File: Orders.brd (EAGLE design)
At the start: 160 x 100 mm, 5 parts, among them J1 10104111-0001LF

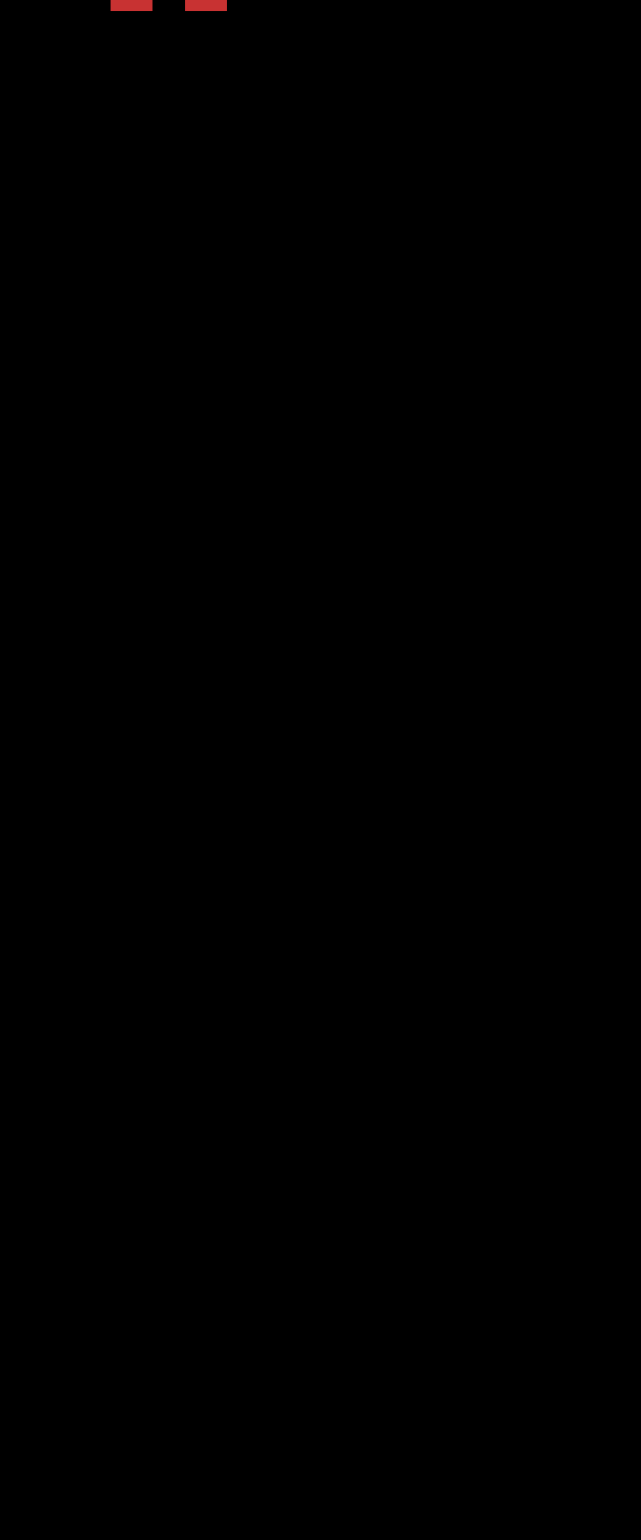
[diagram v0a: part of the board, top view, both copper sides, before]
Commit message: Added I2C pull-up resistances
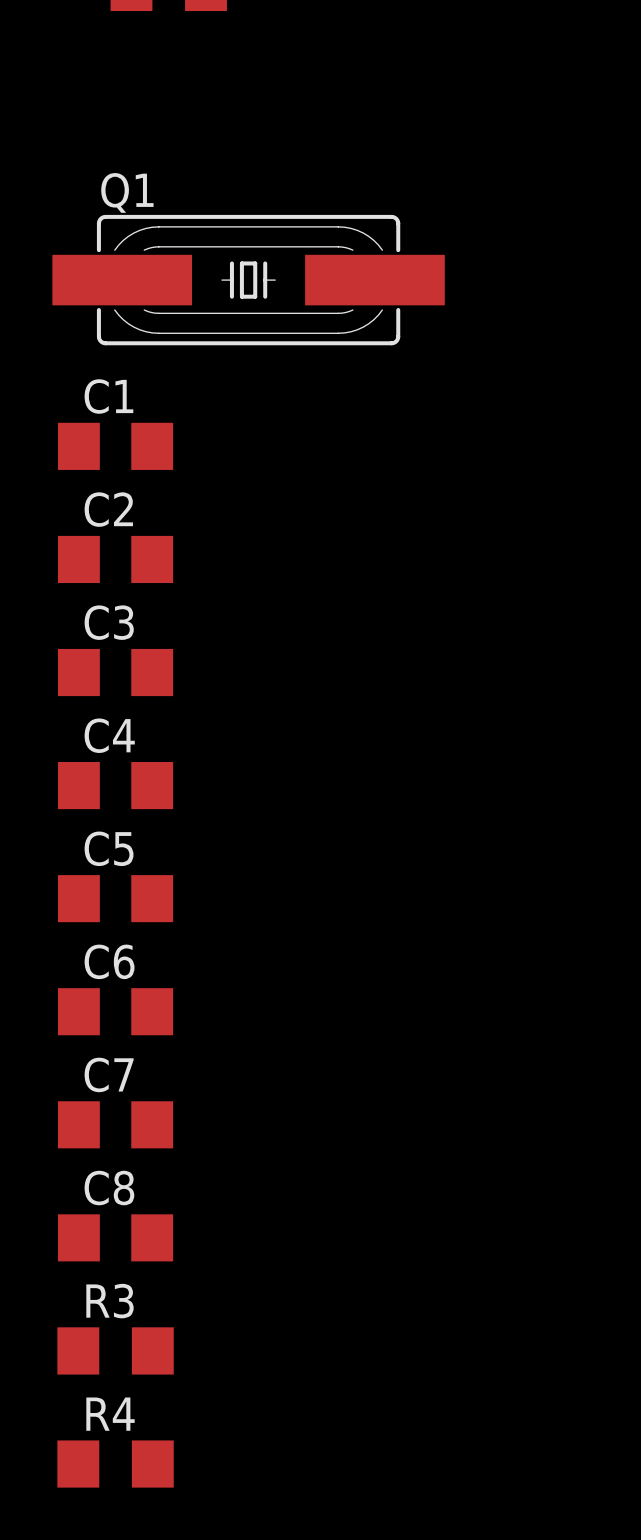
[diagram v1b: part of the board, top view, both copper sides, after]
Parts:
- added C1, C2, C3, C4, C5, C6, C7, C8: (no value), rcl:C1206
- added Q1: (no value), adafruit:HC49UP
- added R3, R4: (no value), rcl:R1206
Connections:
- new net N$3: C1.1, Q1.2, U$1.17
- new net N$4: C2.1, Q1.1, U$1.16
- new net N$5: C3.1, U$1.6
- net +5V: now also C4.1, C5.1, C6.1, C7.1, C8.1, R3.2, R4.2, U$1.14, U$1.2, U$1.24, U$1.34, U$1.44, U$1.7
- net D+: now also U$1.4
- net D-: now also U$1.3
- net GND: now also C1.2, C2.2, C3.2, C4.2, C5.2, C6.2, C7.2, C8.2, U$1.15, U$1.23, U$1.35, U$1.43, U$1.5
- net SCL: now also R3.1
- net SDA: now also R4.1

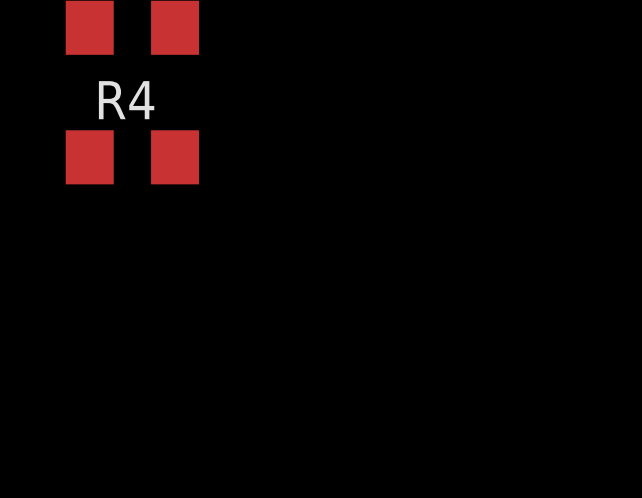
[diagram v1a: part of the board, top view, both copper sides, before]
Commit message: Added passives for uC
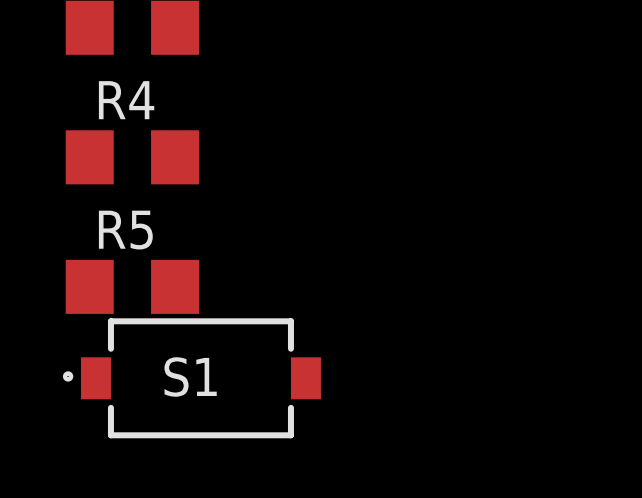
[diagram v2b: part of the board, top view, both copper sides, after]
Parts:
- added R5: (no value), rcl:R1206
- added S1: KSR231GLFS, Switch:KSR
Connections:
- new net N$6: R5.2, S1.2, U$1.13
- net +5V: now also R5.1
- net GND: now also S1.1
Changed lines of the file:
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@@
 <attribute name="VALUE" x="-50.292" y="-81.788" size="1.27" layer="27"/>
+</element>
+<element name="R5" library="rcl" library_urn="urn:adsk.eagle:library:334" package="R1206" package3d_urn="urn:adsk.eagle:package:23540/2" value="" x="-49.022" y="-83.566" smashed="yes">
+<attribute name="NAME" x="-50.292" y="-82.296" size="1.27" layer="25"/>
+<attribute name="POPULARITY" value="41" x="-49.022" y="-83.566" size="1.778" layer="27" display="off"/>
+<attribute name="SPICEPREFIX" value="R" x="-49.022" y="-83.566" size="1.778" layer="27" display="off"/>
+<attribute name="VALUE" x="-50.292" y="-86.106" size="1.27" layer="27"/>
+</element>
+<element name="S1" library="Switch" package="KSR" value="KSR231GLFS" x="-46.736" y="-86.614" smashed="yes">
+<attribute name="DESCRIPTION" value="Switch Tactile SMT gull wing 3.0N silver IP50 Tactile Switch, SPST-NO 50 mA dc 0.75mm" x="-46.736" y="-86.614" size="1.778" layer="27" display="off"/>
+<attribute name="HEIGHT" value="mm" x="-46.736" y="-86.614" size="1.778" layer="27" display="off"/>
+<attribute name="MANUFACTURER_NAME" value="C &amp; K COMPONENTS" x="-46.736" y="-86.614" size="1.778" layer="27" display="off"/>
+<attribute name="MANUFACTURER_PART_NUMBER" value="KSR231GLFS" x="-46.736" y="-86.614" size="1.778" layer="27" display="off"/>
+<attribute name="MOUSER_PART_NUMBER" value="611-KSR231GLFS" x="-46.736" y="-86.614" size="1.778" layer="27" display="off"/>
+<attribute name="MOUSER_PRICE-STOCK" value="https://www.mouser.com/Search/Refine.aspx?Keyword=611-KSR231GLFS" x="-46.736" y="-86.614" size="1.778" layer="27" display="off"/>
+<attribute name="NAME" x="-47.060809375" y="-86.56933125" size="1.27" layer="25" align="center"/>
+<attribute name="RS_PART_NUMBER" value="7931673P" x="-46.736" y="-86.614" size="1.778" layer="27" display="off"/>
+<attribute name="RS_PRICE-STOCK" value="http://uk.rs-online.com/web/p/products/7931673P" x="-46.736" y="-86.614" size="1.778" layer="27" display="off"/>
+<attribute name="VALUE" x="-47.060809375" y="-79.96533125" size="1.27" layer="27" align="center"/>
 </element>
 </elements>
@@
 <contactref element="R4" pad="2"/>
 <contactref element="R3" pad="2"/>
+<contactref element="R5" pad="1"/>
+<wire x1="-47.6" y1="-79.248" x2="-50.444" y2="-83.566" width="0" layer="19" extent="1-1"/>
 <wire x1="-47.6" y1="-74.93" x2="-47.6" y2="-79.248" width="0" layer="19" extent="1-1"/>
 <wire x1="-50.422" y1="-70.612" x2="-47.6" y2="-74.93" width="0" layer="19" extent="1-1"/>
@@
 <contactref element="C7" pad="2"/>
 <contactref element="C8" pad="2"/>
+<contactref element="S1" pad="1"/>
+<wire x1="-47.622" y1="-70.612" x2="-50.236" y2="-86.614" width="0" layer="19" extent="1-1"/>
 <wire x1="-47.622" y1="-66.294" x2="-47.622" y2="-70.612" width="0" layer="19" extent="1-1"/>
 <wire x1="-47.622" y1="-61.976" x2="-47.622" y2="-66.294" width="0" layer="19" extent="1-1"/>
@@
 <wire x1="-47.71" y1="10.16" x2="-50.422" y2="-49.022" width="0" layer="19" extent="1-1"/>
 </signal>
+<signal name="N$6">
+<contactref element="S1" pad="2"/>
+<contactref element="U$1" pad="13"/>
+<contactref element="R5" pad="2"/>
+<wire x1="-47.6" y1="-83.566" x2="-43.236" y2="-86.614" width="0" layer="19" extent="1-1"/>
+<wire x1="-45.11" y1="4.36" x2="-47.6" y2="-83.566" width="0" layer="19" extent="1-1"/>
+</signal>
 </signals>

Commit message: Finished schematic
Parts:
- added JP2: (no value), pinhead:1X06
- moved U$1 131.9 mm to (80.0, 60.5)
- moved J1 122.5 mm to (80.3, 1.78)
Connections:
- new net RX: JP2.4, U$1.20
- new net TX: JP2.5, U$1.21
- net +5V: now also JP2.2
- net GND: now also JP2.3
- net SCL: now also U$1.18
- net SDA: now also U$1.19

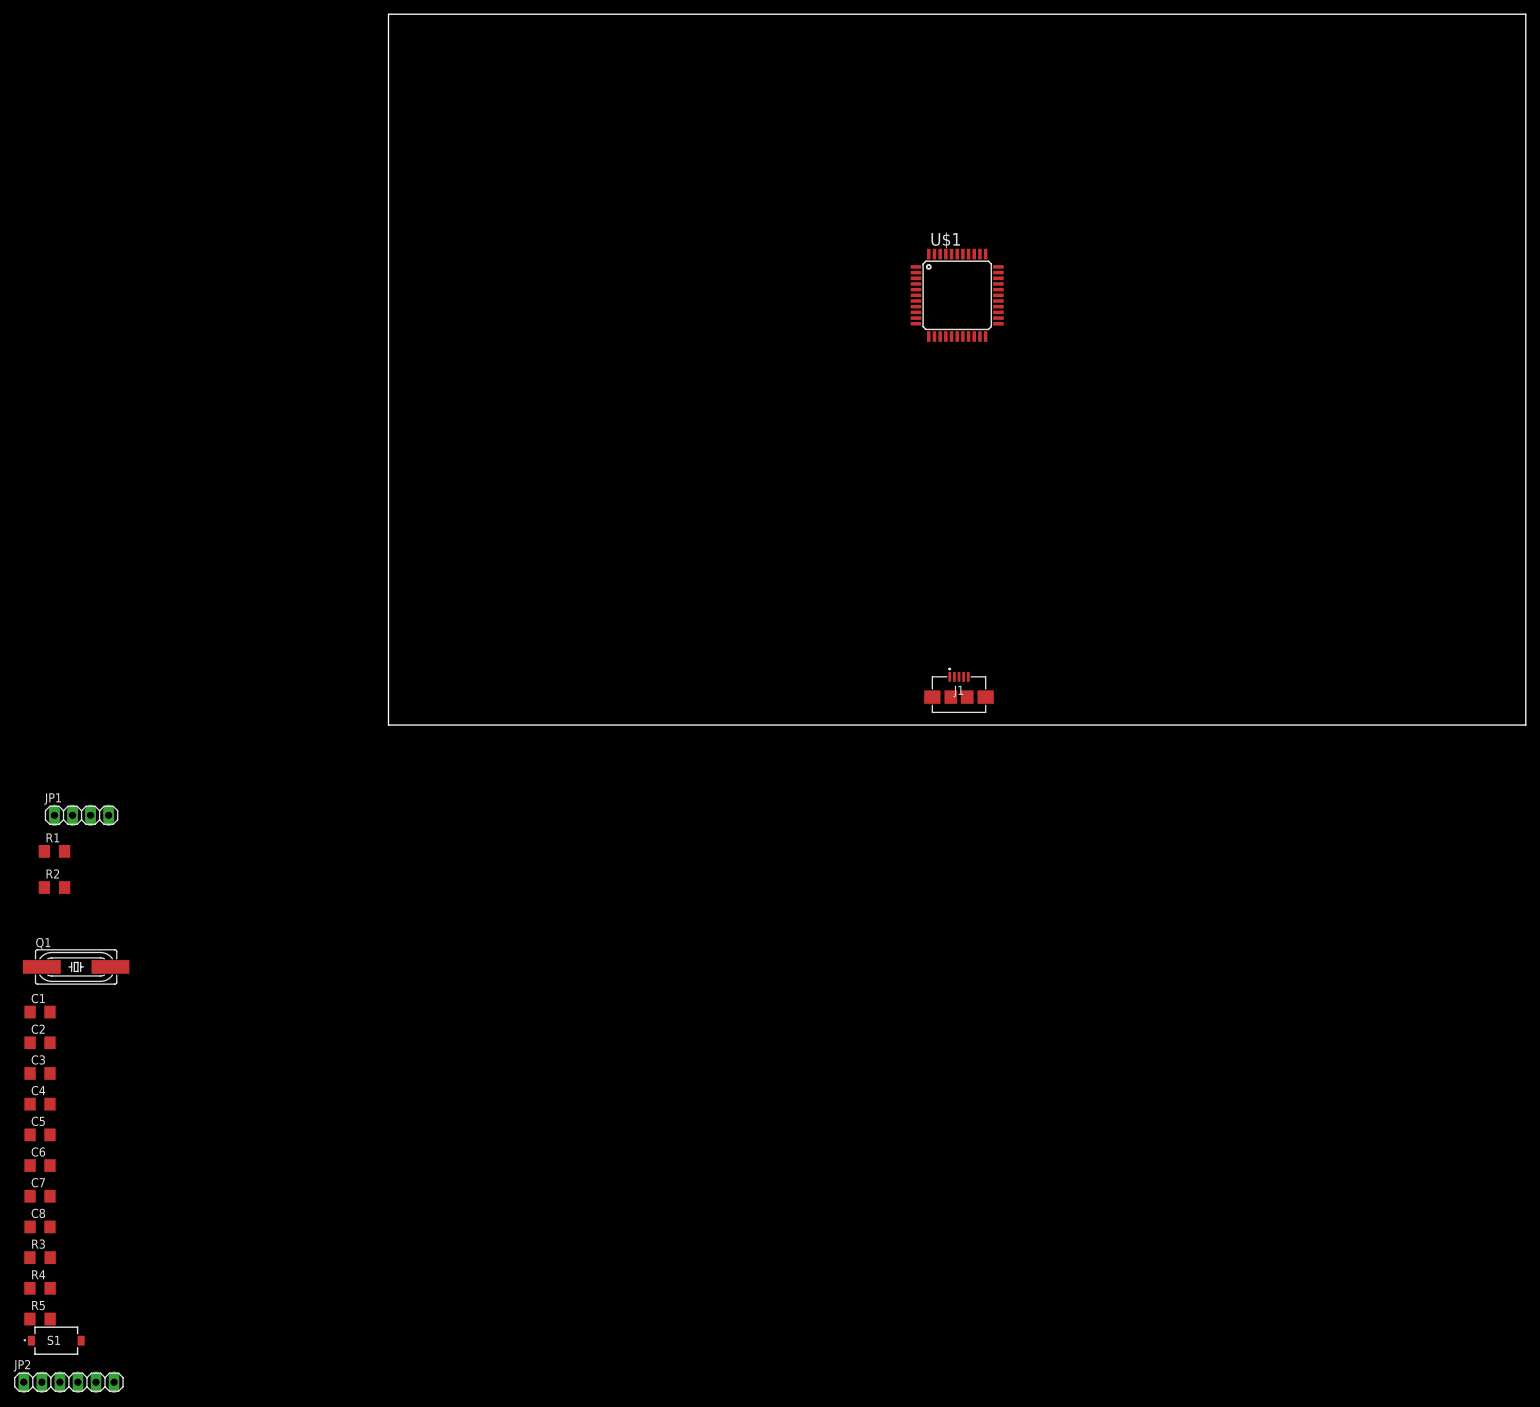
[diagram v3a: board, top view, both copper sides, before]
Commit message: Refined ground planes
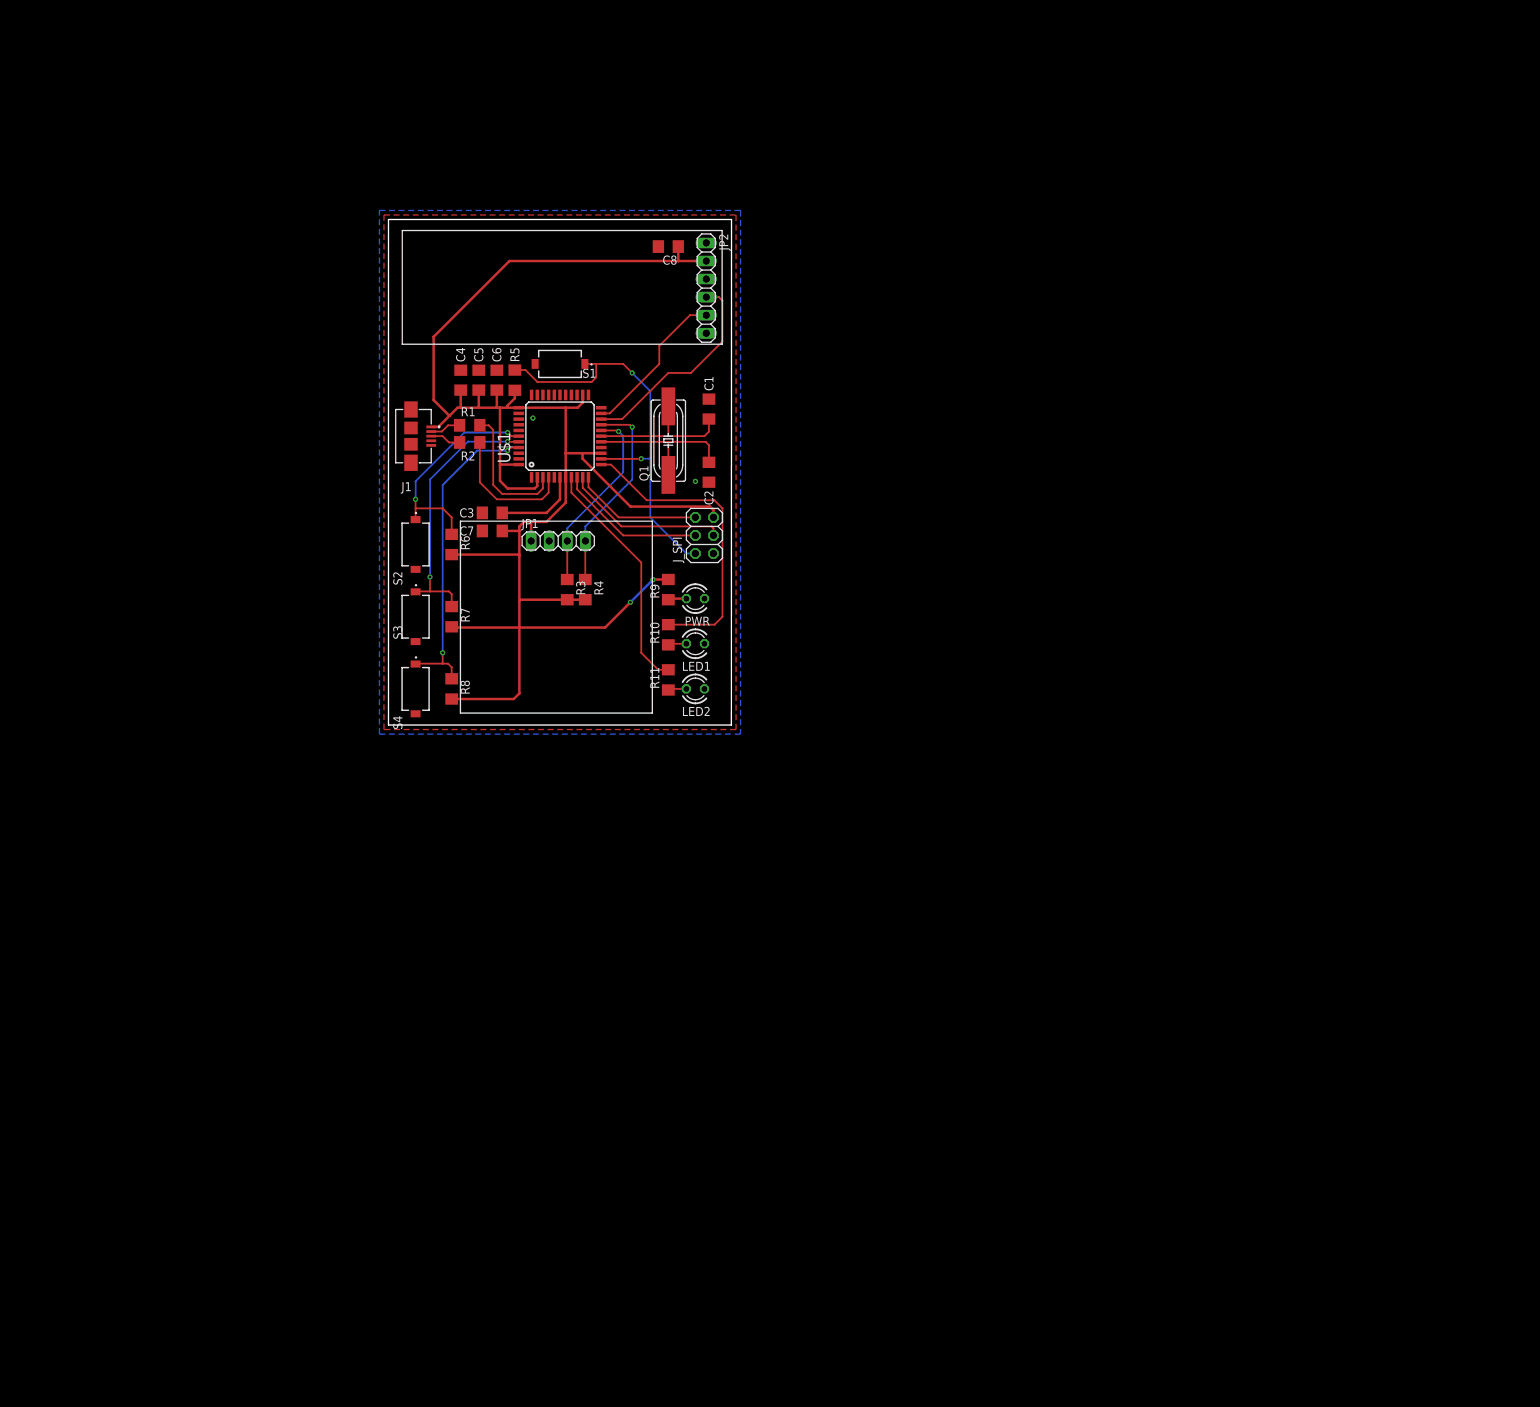
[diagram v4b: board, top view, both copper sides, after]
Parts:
- added J_SPI: (no value), pinhead:2X03
- added LED1, LED2, PWR: (no value), led:LED3MM
- added R10, R11, R6, R7, R8, R9: (no value), rcl:R1206
- added S2, S3, S4: KSR231GLFS, Switch:KSR
- moved JP2 178.1 mm to (44.7, 61.5), turned to 270 degrees
- moved C8 163.8 mm to (39.4, 67.3), turned to 180 degrees
- moved S1 154.6 mm to (24.1, 50.8), turned to 180 degrees
- moved R5 148.0 mm to (17.8, 48.5), turned to 90 degrees
- moved C6 127.8 mm to (15.2, 48.5), turned to 90 degrees
- moved C1 126.7 mm to (45.1, 44.5), turned to 90 degrees
- moved R4 124.7 mm to (27.7, 19.1), turned to 270 degrees
- moved C2 123.7 mm to (45.1, 35.6), turned to 270 degrees
- moved C5 122.8 mm to (12.7, 48.5), turned to 90 degrees
- moved R3 119.7 mm to (25.1, 19.1), turned to 270 degrees
- moved C4 117.8 mm to (10.2, 48.5), turned to 90 degrees
- moved C7 113.2 mm to (14.6, 27.3), turned to 180 degrees
- moved Q1 111.5 mm to (39.4, 40.0), turned to 90 degrees
- moved C3 101.3 mm to (14.6, 29.8), turned to 180 degrees
- moved J1 88.3 mm to (1.02, 40.6), turned to 270 degrees
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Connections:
- net N$5 renamed UCAP
- new net L1: R10.2, U$1.12
- new net L2: R11.2, U$1.8
- new net MISO: J_SPI.1, U$1.11
- new net MOSI: J_SPI.4, U$1.10
- new net N$5: PWR.A, R9.1
- new net N$7: LED2.A, R11.1
- new net RST: J_SPI.5, R5.2, S1.1, U$1.13
- new net SCK: J_SPI.3, U$1.9
- new net TACT_1: R6.1, S2.1, U$1.39
- new net TACT_2: R7.1, S3.1, U$1.40
- new net TACT_3: R8.1, S4.1, U$1.41
- net +5V: now also J_SPI.2, R6.2, R7.2, R8.2, R9.2
- net GND: now also J_SPI.6, LED1.K, LED2.K, PWR.K, S1.2, S2.2, S3.2, S4.2; no longer S1.1
- net N$6: now also LED1.A, R10.1; no longer R5.2, S1.2, U$1.13
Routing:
- net +5V: track 0.00 -> 251.1 mm, vias 0 -> 2
- net RST: track 0.00 -> 58.3 mm, vias 0 -> 2
- net TACT_3: track 0.00 -> 45.0 mm, vias 0 -> 2
- net L1: track 0.00 -> 42.9 mm
- net TACT_2: track 0.00 -> 37.5 mm, vias 0 -> 2
- net L2: track 0.00 -> 33.6 mm
- net TACT_1: track 0.00 -> 31.0 mm, vias 0 -> 2
- net RX: track 0.00 -> 29.8 mm
- net SDA: track 0.00 -> 28.7 mm, vias 0 -> 1
- net SCL: track 0.00 -> 26.9 mm, vias 0 -> 1
- net MOSI: track 0.00 -> 23.2 mm
- net N$4: track 0.00 -> 22.4 mm
- net TX: track 0.00 -> 22.0 mm
- net N$3: track 0.00 -> 21.4 mm
- net SCK: track 0.00 -> 21.0 mm
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- added copper zone on layer 1, net GND
- added copper zone on layer 16, net GND
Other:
- board size 160 x 100 mm -> 48.3 x 71.1 mm

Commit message: Final commit, added software
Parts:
- renumbered S1 to RST, S2 to UP, S3 to OK, S4 to DOWN, U$1 to U1
